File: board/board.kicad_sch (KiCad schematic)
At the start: 4 parts, among them J1 008_USB_2x2, J2 009_1000BASE-T_2x5, U3 TC1017-xCT

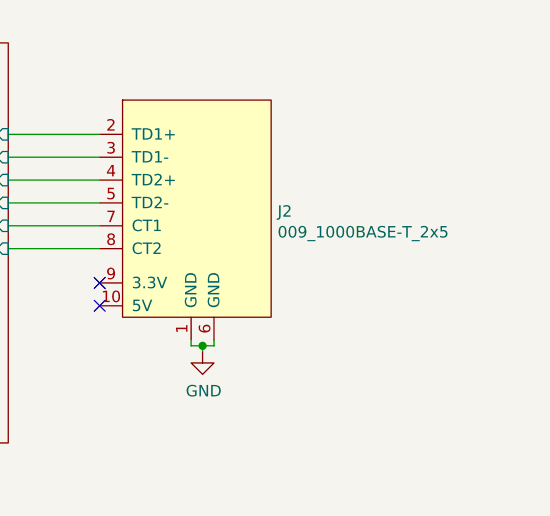
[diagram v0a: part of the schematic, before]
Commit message: changed osf.009 to osf.019 on silkscreen
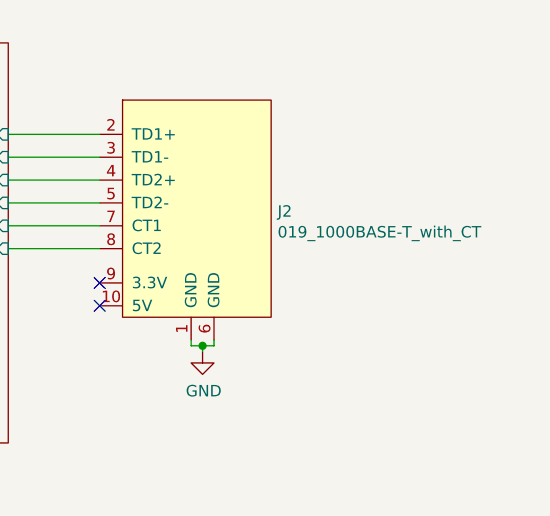
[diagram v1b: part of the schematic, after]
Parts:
- J2: value 009_1000BASE-T_2x5 -> 019_1000BASE-T_with_CT
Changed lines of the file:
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@@
       (effects (font (size 1.27 1.27)) (justify left))
     )
-    (property "Value" "009_1000BASE-T_2x5" (id 1) (at 182.3212 84.5312 0)
+    (property "Value" "019_1000BASE-T_with_CT" (id 1) (at 182.3212 84.5312 0)
       (effects (font (size 1.27 1.27)) (justify left))
     )
@@
     )
     (path "/00000000-0000-0000-0000-00006036f103"
-      (reference "J2") (unit 1) (value "009_1000BASE-T_2x5") (footprint "on_edge:on_edge_2x05_host")
+      (reference "J2") (unit 1) (value "019_1000BASE-T_with_CT") (footprint "on_edge:on_edge_2x05_host")
     )
     (path "/00000000-0000-0000-0000-0000603703e4/00000000-0000-0000-0000-00005f44cffe"
